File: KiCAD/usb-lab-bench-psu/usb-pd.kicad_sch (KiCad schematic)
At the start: 21 parts, among them J1 USB_PD_Receptacle, Q1 PMOS, Q2 PMOS, U1 STUSB4500QTR

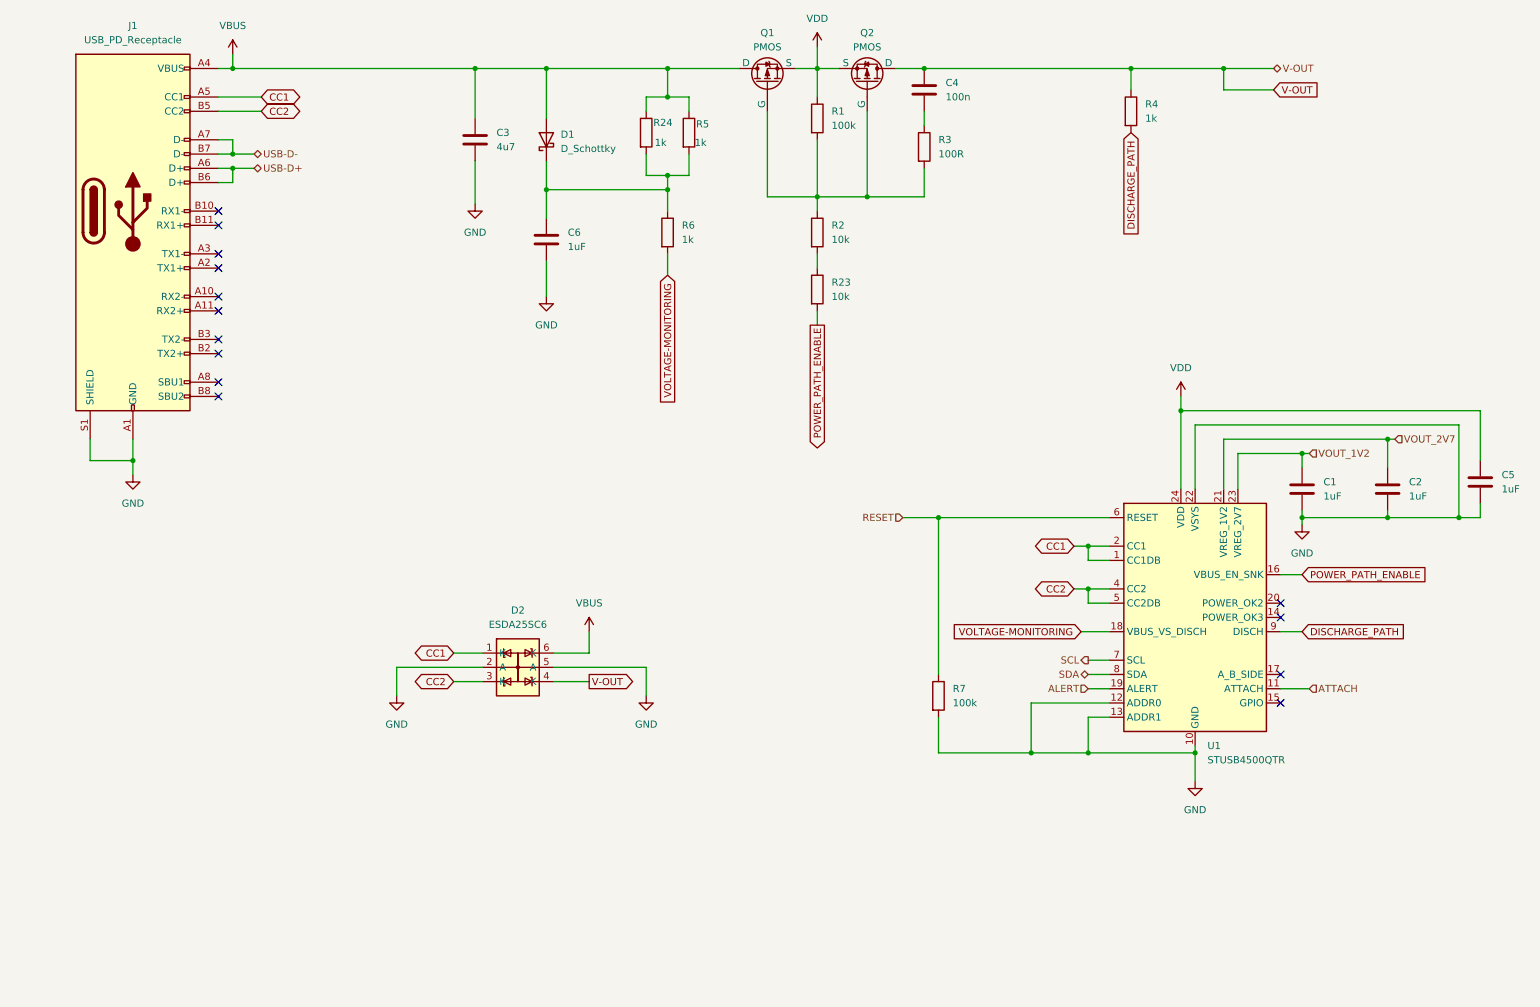
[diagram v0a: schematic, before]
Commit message: Replaced global labels with labels, added measurement circuit, started with io board
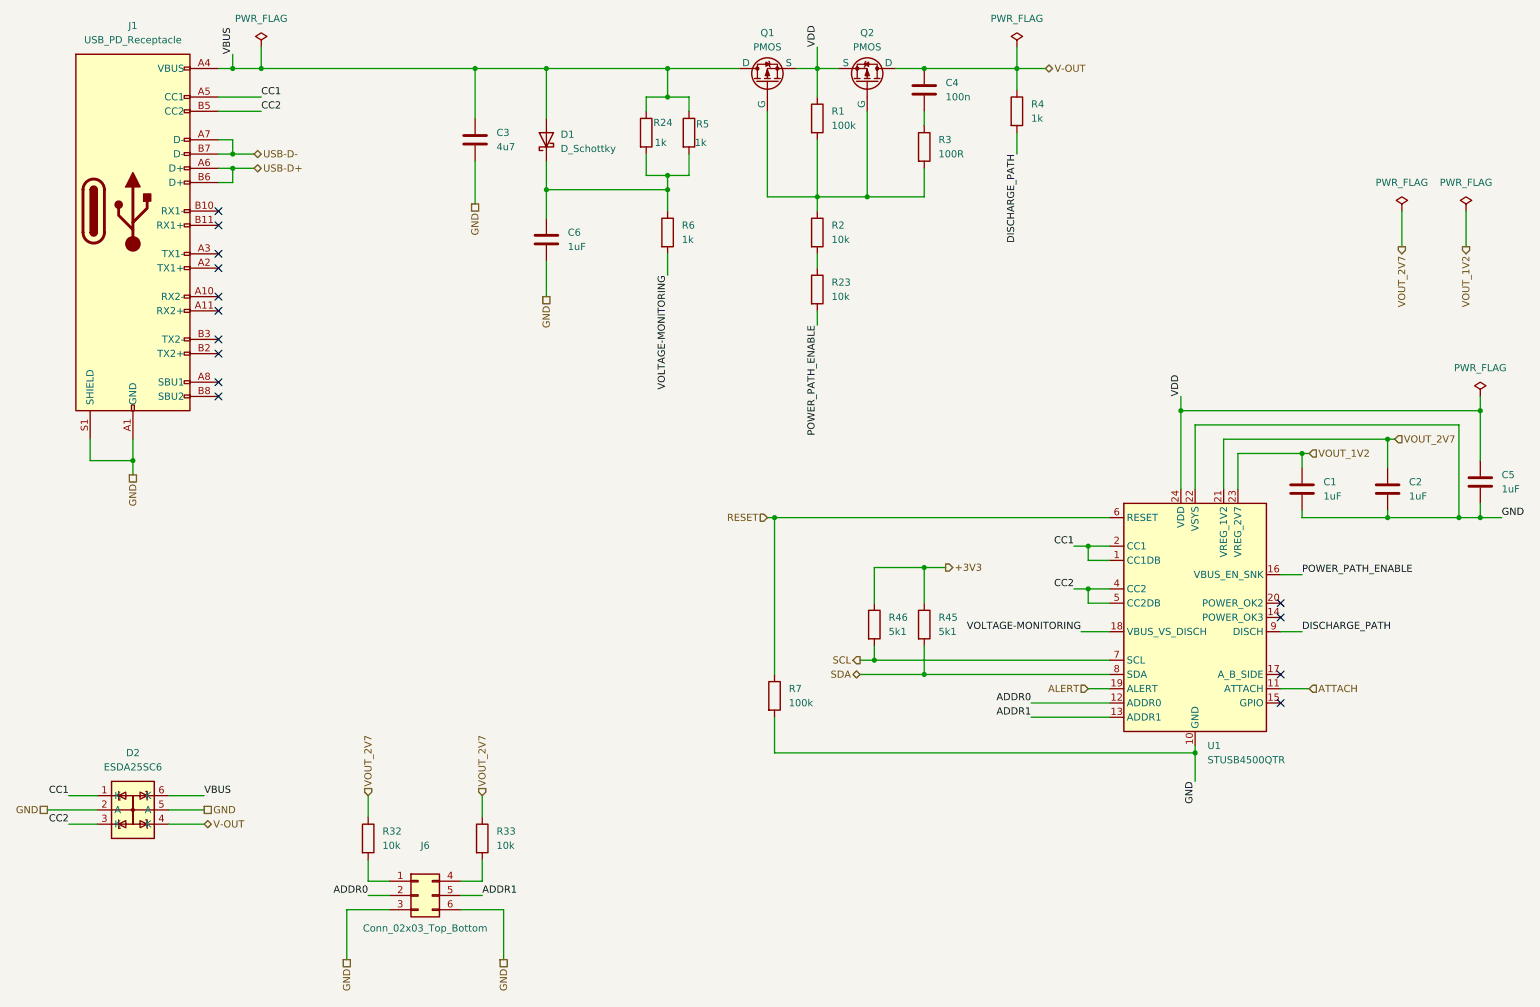
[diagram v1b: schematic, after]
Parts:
- added J6: Conn_02x03_Top_Bottom, symbol Connector_Generic:Conn_02x03_Top_Bottom
- added R32, R33: 10k, symbol Device:R
- added R45, R46: 5k1, symbol Device:R
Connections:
- net GND: now also J6.3 (Pin_3), J6.6 (Pin_6); no longer U1.12 (ADDR0), U1.13 (ADDR1)
- net SCL: now also R46.2
- net SDA: now also R45.2
- net VOUT_2V7: now also R32.1, R33.1
- new net: J6.4 (Pin_4), R33.2
- new net: J6.1 (Pin_1), R32.2
- new net +3V3: R45.1, R46.1
- new net ADDR0: J6.2 (Pin_2), U1.12 (ADDR0)
- new net ADDR1: J6.5 (Pin_5), U1.13 (ADDR1)
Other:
- moved on the sheet: D2, R4, R7

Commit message: updated GND and supply nets, switched buck-boost-converter
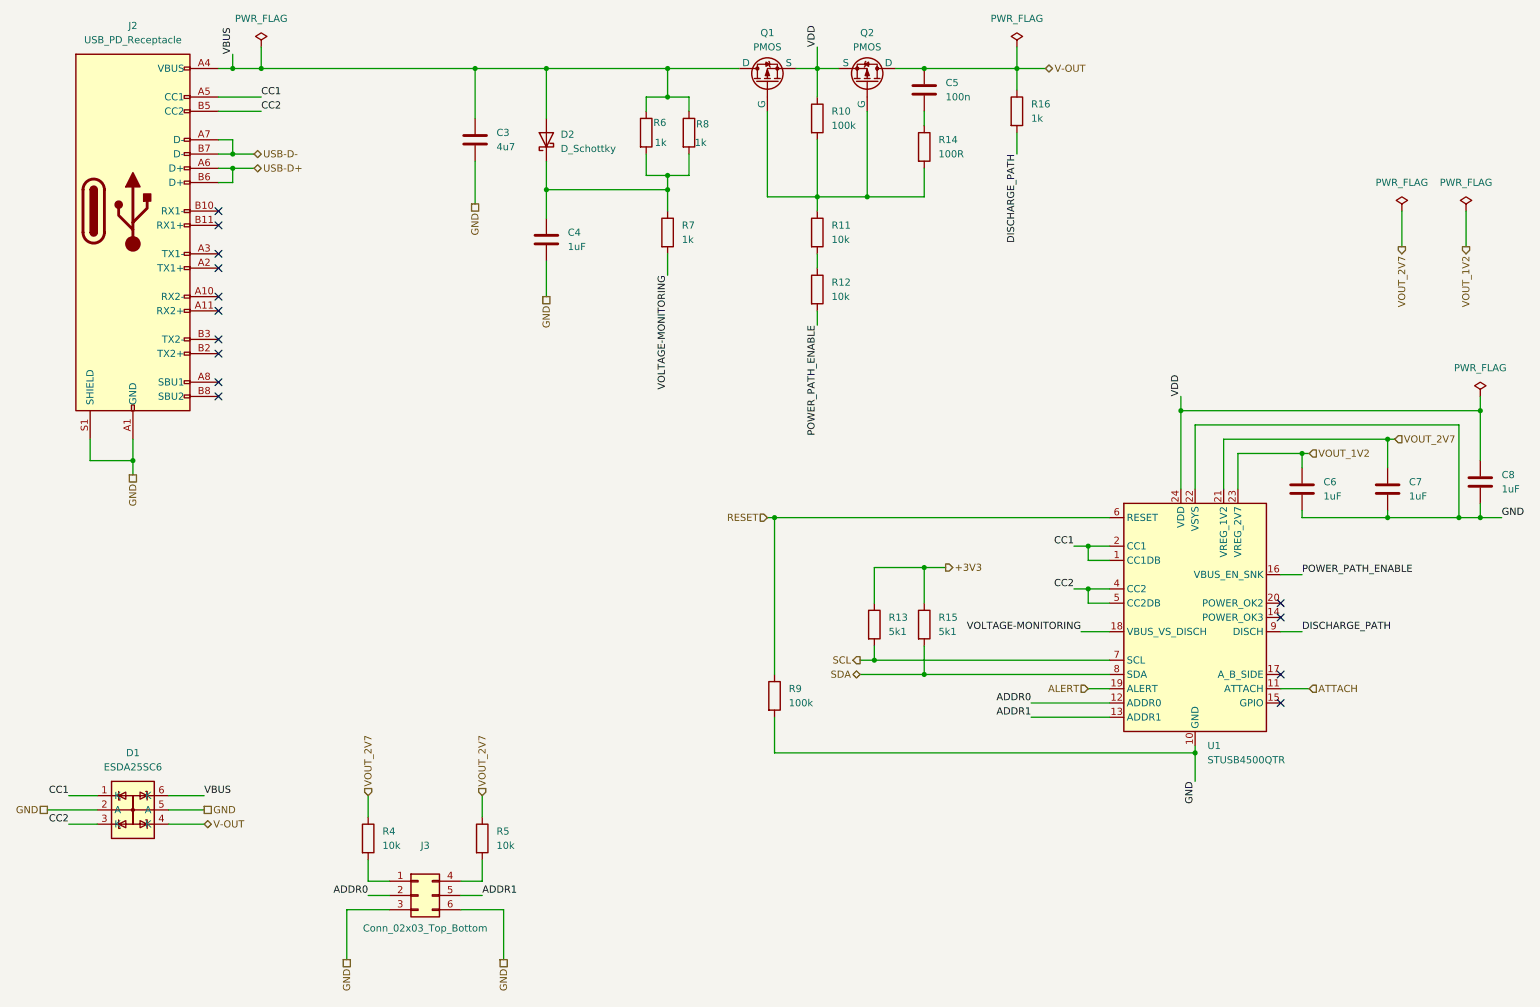
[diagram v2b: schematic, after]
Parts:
- renumbered C6 to C4, C4 to C5, C1 to C6, C2 to C7, C5 to C8, D2 to D1, D1 to D2, J1 to J2, J6 to J3, R1 to R10, R2 to R11, R23 to R12, R46 to R13, R3 to R14, R45 to R15, R4 to R16, R32 to R4, R33 to R5, R24 to R6, R6 to R7, R5 to R8, R7 to R9
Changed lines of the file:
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@@
 		(dnp no)
 		(fields_autoplaced yes)
-		(property "Reference" "R4"
+		(property "Reference" "R16"
 			(at 196.85 34.2899 0)
 			(effects
@@
 			(project "usb-lab-bench-psu"
 				(path "/63928bc9-e618-488a-a687-c6d5597f31d9/cc314cc1-26b0-4e6c-b14c-ea7785b99358"
-					(reference "R4")
+					(reference "R16")
 					(unit 1)
 				)
@@
 		(dnp no)
 		(fields_autoplaced yes)
-		(property "Reference" "R33"
+		(property "Reference" "R5"
 			(at 101.6 163.8299 0)
 			(effects
@@
 			(project "usb-lab-bench-psu"
 				(path "/63928bc9-e618-488a-a687-c6d5597f31d9/cc314cc1-26b0-4e6c-b14c-ea7785b99358"
-					(reference "R33")
+					(reference "R5")
 					(unit 1)
 				)
@@
 		(dnp no)
 		(fields_autoplaced yes)
-		(property "Reference" "R2"
+		(property "Reference" "R11"
 			(at 161.29 55.8799 0)
 			(effects
@@
 			(project ""
 				(path "/63928bc9-e618-488a-a687-c6d5597f31d9/cc314cc1-26b0-4e6c-b14c-ea7785b99358"
-					(reference "R2")
+					(reference "R11")
 					(unit 1)
 				)
@@
 		(dnp no)
 		(fields_autoplaced yes)
-		(property "Reference" "R6"
+		(property "Reference" "R7"
 			(at 134.62 55.8799 0)
 			(effects
@@
 			(project "usb-lab-bench-psu"
 				(path "/63928bc9-e618-488a-a687-c6d5597f31d9/cc314cc1-26b0-4e6c-b14c-ea7785b99358"
-					(reference "R6")
+					(reference "R7")
 					(unit 1)
 				)
@@
 		(dnp no)
 		(fields_autoplaced yes)
-		(property "Reference" "R1"
+		(property "Reference" "R10"
 			(at 161.29 35.5599 0)
 			(effects
@@
 			(project ""
 				(path "/63928bc9-e618-488a-a687-c6d5597f31d9/cc314cc1-26b0-4e6c-b14c-ea7785b99358"
-					(reference "R1")
+					(reference "R10")
 					(unit 1)
 				)
@@
 		(on_board yes)
 		(dnp no)
-		(property "Reference" "J6"
+		(property "Reference" "J3"
 			(at 88.9 166.37 0)
 			(effects
@@
 			(project ""
 				(path "/63928bc9-e618-488a-a687-c6d5597f31d9/cc314cc1-26b0-4e6c-b14c-ea7785b99358"
-					(reference "J6")
+					(reference "J3")
 					(unit 1)
 				)
@@
 		(dnp no)
 		(fields_autoplaced yes)
-		(property "Reference" "D2"
+		(property "Reference" "D1"
 			(at 36.83 149.86 0)
 			(effects
@@
 			(project ""
 				(path "/63928bc9-e618-488a-a687-c6d5597f31d9/cc314cc1-26b0-4e6c-b14c-ea7785b99358"
-					(reference "D2")
+					(reference "D1")
 					(unit 1)
 				)
@@
 		(dnp no)
 		(fields_autoplaced yes)
-		(property "Reference" "C2"
+		(property "Reference" "C7"
 			(at 264.16 101.5999 0)
 			(effects
@@
 			(project "usb-lab-bench-psu"
 				(path "/63928bc9-e618-488a-a687-c6d5597f31d9/cc314cc1-26b0-4e6c-b14c-ea7785b99358"
-					(reference "C2")
+					(reference "C7")
 					(unit 1)
 				)
@@
 		(dnp no)
 		(fields_autoplaced yes)
-		(property "Reference" "D1"
+		(property "Reference" "D2"
 			(at 113.03 39.6874 90)
 			(effects
@@
 			(project ""
 				(path "/63928bc9-e618-488a-a687-c6d5597f31d9/cc314cc1-26b0-4e6c-b14c-ea7785b99358"
-					(reference "D1")
+					(reference "D2")
 					(unit 1)
 				)
@@
 		(dnp no)
 		(fields_autoplaced yes)
-		(property "Reference" "C4"
+		(property "Reference" "C5"
 			(at 181.61 30.4799 0)
 			(effects
@@
 			(project ""
 				(path "/63928bc9-e618-488a-a687-c6d5597f31d9/cc314cc1-26b0-4e6c-b14c-ea7785b99358"
-					(reference "C4")
+					(reference "C5")
 					(unit 1)
 				)
@@
 		(on_board yes)
 		(dnp no)
-		(property "Reference" "R24"
+		(property "Reference" "R6"
 			(at 129.54 37.592 0)
 			(effects
@@
 			(project "usb-lab-bench-psu"
 				(path "/63928bc9-e618-488a-a687-c6d5597f31d9/cc314cc1-26b0-4e6c-b14c-ea7785b99358"
-					(reference "R24")
+					(reference "R6")
 					(unit 1)
 				)
@@
 		(dnp no)
 		(fields_autoplaced yes)
-		(property "Reference" "J1"
+		(property "Reference" "J2"
 			(at 36.83 20.32 0)
 			(effects
@@
 			(project ""
 				(path "/63928bc9-e618-488a-a687-c6d5597f31d9/cc314cc1-26b0-4e6c-b14c-ea7785b99358"
-					(reference "J1")
+					(reference "J2")
 					(unit 1)
 				)
@@
 		(on_board yes)
 		(dnp no)
-		(property "Reference" "R5"
+		(property "Reference" "R8"
 			(at 137.16 37.846 0)
 			(effects
@@
 			(project "usb-lab-bench-psu"
 				(path "/63928bc9-e618-488a-a687-c6d5597f31d9/cc314cc1-26b0-4e6c-b14c-ea7785b99358"
-					(reference "R5")
+					(reference "R8")
 					(unit 1)
 				)
@@
 		(dnp no)
 		(fields_autoplaced yes)
-		(property "Reference" "C6"
+		(property "Reference" "C4"
 			(at 114.3 57.1499 0)
 			(effects
@@
 			(project "usb-lab-bench-psu"
 				(path "/63928bc9-e618-488a-a687-c6d5597f31d9/cc314cc1-26b0-4e6c-b14c-ea7785b99358"
-					(reference "C6")
+					(reference "C4")
 					(unit 1)
 				)
@@
 		(dnp no)
 		(fields_autoplaced yes)
-		(property "Reference" "#FLG04"
+		(property "Reference" "#FLG03"
 			(at 262.89 51.435 0)
 			(effects
@@
 			(project "usb-lab-bench-psu"
 				(path "/63928bc9-e618-488a-a687-c6d5597f31d9/cc314cc1-26b0-4e6c-b14c-ea7785b99358"
-					(reference "#FLG04")
+					(reference "#FLG03")
 					(unit 1)
 				)
@@
 		(dnp no)
 		(fields_autoplaced yes)
-		(property "Reference" "R3"
+		(property "Reference" "R14"
 			(at 180.34 40.6399 0)
 			(effects
@@
 			(project ""
 				(path "/63928bc9-e618-488a-a687-c6d5597f31d9/cc314cc1-26b0-4e6c-b14c-ea7785b99358"
-					(reference "R3")
+					(reference "R14")
 					(unit 1)
 				)
@@
 		(dnp no)
 		(fields_autoplaced yes)
-		(property "Reference" "R45"
+		(property "Reference" "R15"
 			(at 180.34 125.7299 0)
 			(effects
@@
 			(project ""
 				(path "/63928bc9-e618-488a-a687-c6d5597f31d9/cc314cc1-26b0-4e6c-b14c-ea7785b99358"
-					(reference "R45")
+					(reference "R15")
 					(unit 1)
 				)
@@
 		(dnp no)
 		(fields_autoplaced yes)
-		(property "Reference" "R23"
+		(property "Reference" "R12"
 			(at 161.29 66.0399 0)
 			(effects
@@
 			(project "usb-lab-bench-psu"
 				(path "/63928bc9-e618-488a-a687-c6d5597f31d9/cc314cc1-26b0-4e6c-b14c-ea7785b99358"
-					(reference "R23")
+					(reference "R12")
 					(unit 1)
 				)
@@
 		(dnp no)
 		(fields_autoplaced yes)
-		(property "Reference" "R7"
+		(property "Reference" "R9"
 			(at 153.67 138.4299 0)
 			(effects
@@
 			(project "usb-lab-bench-psu"
 				(path "/63928bc9-e618-488a-a687-c6d5597f31d9/cc314cc1-26b0-4e6c-b14c-ea7785b99358"
-					(reference "R7")
+					(reference "R9")
 					(unit 1)
 				)
@@
 		(dnp no)
 		(fields_autoplaced yes)
-		(property "Reference" "R46"
+		(property "Reference" "R13"
 			(at 171.45 125.7299 0)
 			(effects
@@
 			(project "usb-lab-bench-psu"
 				(path "/63928bc9-e618-488a-a687-c6d5597f31d9/cc314cc1-26b0-4e6c-b14c-ea7785b99358"
-					(reference "R46")
+					(reference "R13")
 					(unit 1)
 				)
@@
 		(dnp no)
 		(fields_autoplaced yes)
-		(property "Reference" "R32"
+		(property "Reference" "R4"
 			(at 81.28 163.8299 0)
 			(effects
@@
 			(project "usb-lab-bench-psu"
 				(path "/63928bc9-e618-488a-a687-c6d5597f31d9/cc314cc1-26b0-4e6c-b14c-ea7785b99358"
-					(reference "R32")
+					(reference "R4")
 					(unit 1)
 				)
@@
 		(dnp no)
 		(fields_autoplaced yes)
-		(property "Reference" "#FLG05"
+		(property "Reference" "#FLG04"
 			(at 274.32 51.435 0)
 			(effects
@@
 			(project "usb-lab-bench-psu"
 				(path "/63928bc9-e618-488a-a687-c6d5597f31d9/cc314cc1-26b0-4e6c-b14c-ea7785b99358"
-					(reference "#FLG05")
+					(reference "#FLG04")
 					(unit 1)
 				)
@@
 		(dnp no)
 		(fields_autoplaced yes)
-		(property "Reference" "C5"
+		(property "Reference" "C8"
 			(at 280.67 100.3299 0)
 			(effects
@@
 			(project "usb-lab-bench-psu"
 				(path "/63928bc9-e618-488a-a687-c6d5597f31d9/cc314cc1-26b0-4e6c-b14c-ea7785b99358"
-					(reference "C5")
+					(reference "C8")
 					(unit 1)
 				)
@@
 		(dnp no)
 		(fields_autoplaced yes)
-		(property "Reference" "#FLG03"
+		(property "Reference" "#FLG05"
 			(at 276.86 84.455 0)
 			(effects
@@
 			(project "usb-lab-bench-psu"
 				(path "/63928bc9-e618-488a-a687-c6d5597f31d9/cc314cc1-26b0-4e6c-b14c-ea7785b99358"
-					(reference "#FLG03")
+					(reference "#FLG05")
 					(unit 1)
 				)
@@
 		(dnp no)
 		(fields_autoplaced yes)
-		(property "Reference" "C1"
+		(property "Reference" "C6"
 			(at 248.92 101.5999 0)
 			(effects
@@
 			(project ""
 				(path "/63928bc9-e618-488a-a687-c6d5597f31d9/cc314cc1-26b0-4e6c-b14c-ea7785b99358"
-					(reference "C1")
-					(unit 1)
-				)
+					(reference "C6")
+					(unit 1)
+				)
